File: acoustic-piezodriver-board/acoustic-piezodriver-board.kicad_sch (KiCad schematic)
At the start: 1 part, among them P301 WJ128V-5.0-3P

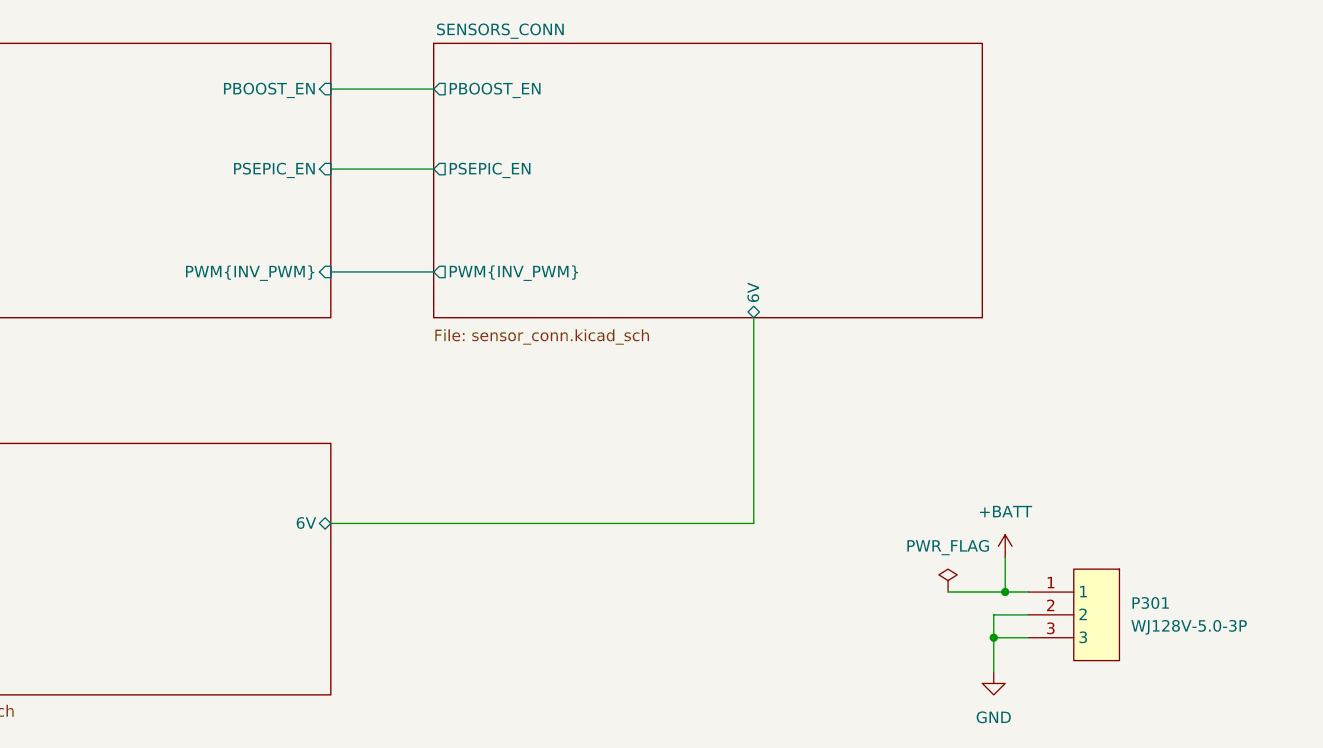
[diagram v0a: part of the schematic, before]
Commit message: [schematic] added adc for temperature measurement, current sense resistors, [layout] component placement, connector placement
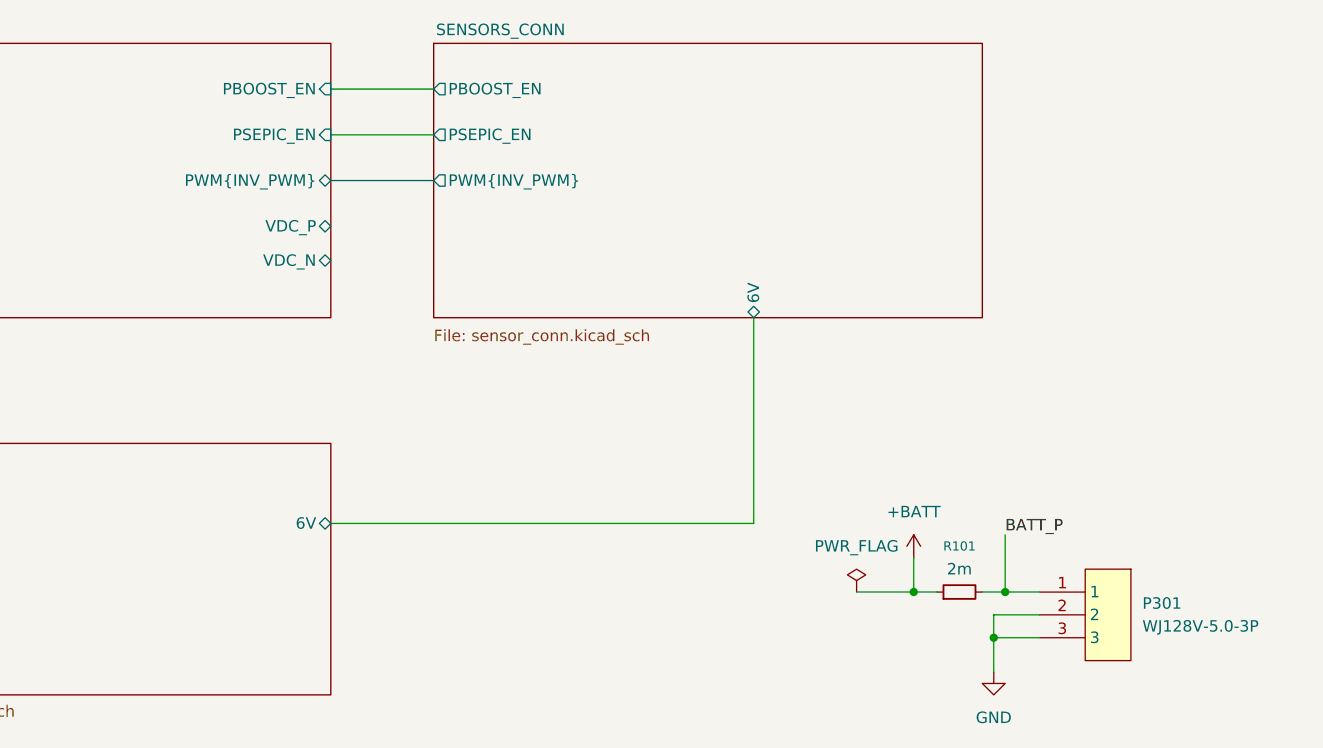
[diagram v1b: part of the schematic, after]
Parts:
- added R101: 2m, Resistor_SMD:R_2512_6332Metric, symbol Device:R_Small
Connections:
- net +BATT: now also R101.1; no longer P301.1
- new net BATT_P: P301.1, R101.2
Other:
- sheet INVERTER ports: added VDC_N, VDC_P; removed none
- moved on the sheet: P301

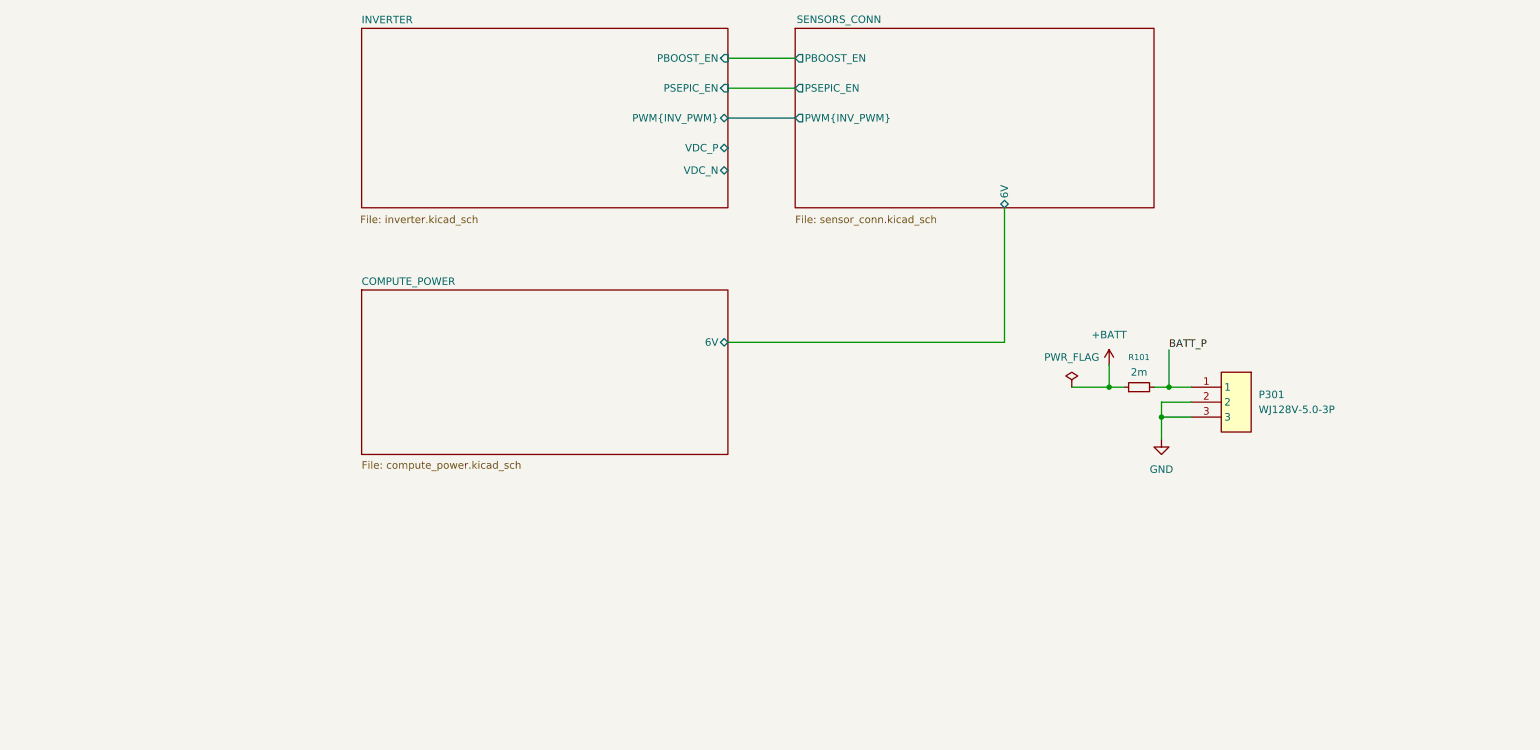
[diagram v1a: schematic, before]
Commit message: found hal-sensor, replaced with different one for lower voltage signal source impedance, reorganised schematic
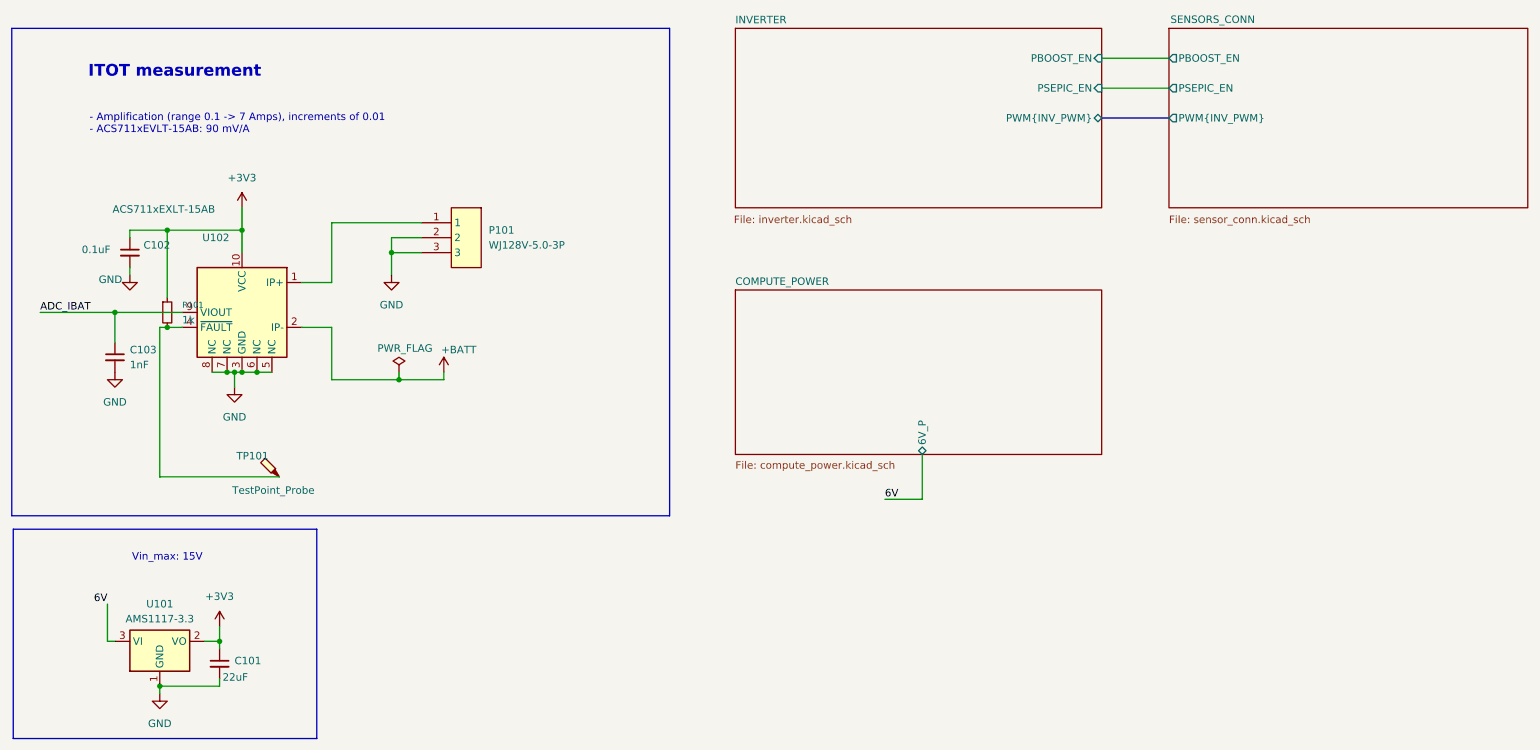
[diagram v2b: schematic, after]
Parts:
- removed P301: WJ128V-5.0-3P, iw-connector:WJ128V-5.0-3P, symbol iw-connector:WJ128V-5.0-3P
- added C101: 22uF, Capacitor_SMD:C_0805_2012Metric, symbol Device:C_Small
- added C102: 0.1uF, Capacitor_SMD:C_0402_1005Metric, symbol Device:C_Small
- added C103: 1nF, Capacitor_SMD:C_0402_1005Metric, symbol Device:C_Small
- added P101: WJ128V-5.0-3P, iw-connector:WJ128V-5.0-3P, symbol iw-connector:WJ128V-5.0-3P
- added TP101: TestPoint_Probe, TestPoint:TestPoint_Pad_D1.0mm, symbol Connector:TestPoint_Probe
- added U101: AMS1117-3.3, Package_TO_SOT_SMD:SOT-223-3_TabPin2, symbol Regulator_Linear:AMS1117-3.3
- added U102: ACS711xEXLT-15AB, Sensor_Current:Allegro_QFN-12-10-1EP_3x3mm_P0.5mm, symbol Sensor_Current:ACS711xEXLT-15AB
- R101: value 2m -> 1k; footprint Resistor_SMD:R_2512_6332Metric -> Resistor_SMD:R_0603_1608Metric; LPN C160590 -> C21190; MPN RLP25FEER002 -> 0603WAF1001T5E
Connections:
- net +BATT: now also U102.2 (IP-); no longer R101.1
- net GND: now also C101.2, C102.2, C103.2, P101.2, P101.3, U101.1 (GND), U102.3 (GND), U102.5 (NC), U102.6 (NC), U102.7 (NC), U102.8 (NC)
- net BATT_P: no longer names the net of R101.2
- net BATT_P: now also TP101.1, U102.4 (~{FAULT})
- new net: P101.1, U102.1 (IP+)
- new net +3V3: C101.1, C102.1, R101.1, U101.2 (VO), U102.10 (VCC)
- new net 6V: U101.3 (VI)
- new net ADC_IBAT: C103.1, U102.9 (VIOUT)
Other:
- sheet COMPUTE_POWER ports: added 6V_P; removed 6V
- sheet INVERTER ports: added none; removed VDC_N, VDC_P
- sheet SENSORS_CONN ports: added none; removed 6V
- note added: "- Amplification (range 0.1 -> 7 Amps), increments of 0.01 - ACS711xEVLT-15AB: 90 mV/A"
- note added: "ITOT measurement"
- note added: "Vin_max: 15V"

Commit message: added new notes + schematic component hal sensors
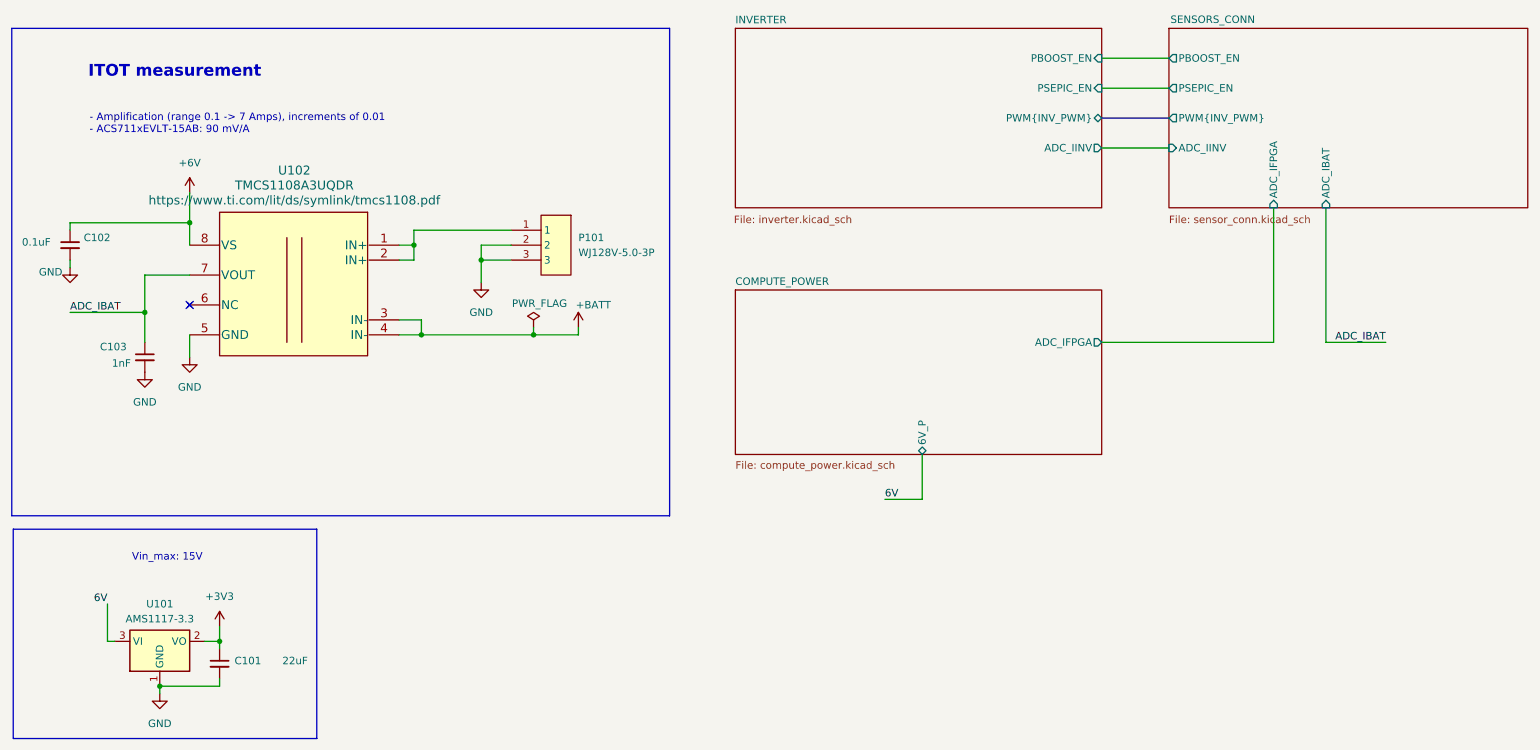
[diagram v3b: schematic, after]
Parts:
- removed R101: 1k, Resistor_SMD:R_0603_1608Metric, symbol Device:R_Small
- removed TP101: TestPoint_Probe, TestPoint:TestPoint_Pad_D1.0mm, symbol Connector:TestPoint_Probe
- removed U102: ACS711xEXLT-15AB, Sensor_Current:Allegro_QFN-12-10-1EP_3x3mm_P0.5mm, symbol Sensor_Current:ACS711xEXLT-15AB
- added U102: TMCS1108A3UQDR, iw-power:TMCS1108A3UQDR, symbol iw-power:TMCS1108A3UQDR
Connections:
- net +3V3: no longer C102.1
- net +BATT: now also U102.3 (IN-), U102.4 (IN-)
- net ADC_IBAT: now also U102.7 (VOUT)
- net GND: now also U102.5 (GND)
- net at P101.1: now also U102.1 (IN+), U102.2 (IN+)
- new net +6V: C102.1, U102.8 (VS)
- no-connect marks 0 -> 1
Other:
- sheet COMPUTE_POWER ports: added ADC_IFPGA; removed none
- sheet INVERTER ports: added ADC_IINV; removed none
- sheet SENSORS_CONN ports: added ADC_IBAT, ADC_IFPGA, ADC_IINV; removed none
- moved on the sheet: C102, C103, P101

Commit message: finished schematic, routing
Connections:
- net 6V is gone; now on net +6V: U101.3 (VI)
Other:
- sheet COMPUTE_POWER ports: added none; removed 6V_P
- note added: "Vin_max: 15V, I_max: 1 A - 2 temperature sensors - 1 ADC"
- note removed: "Vin_max: 15V"
- moved on the sheet: C101, U101
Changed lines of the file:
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@@
 	(paper "A4")
 	(rectangle
-		(start 18.288 130.81)
-		(end 69.85 166.37)
+		(start 18.288 128.27)
+		(end 69.85 163.83)
 		(stroke
 			(width 0)
@@
 	(rectangle
 		(start 18.034 45.72)
-		(end 129.794 128.524)
+		(end 129.794 118.11)
 		(stroke
 			(width 0)
@@
 		)
 	)
-	(text "Vin_max: 15V"
-		(exclude_from_sim no)
-		(at 44.45 135.636 0)
+	(text "Vin_max: 15V, I_max: 1 A\n- 2 temperature sensors\n- 1 ADC"
+		(exclude_from_sim no)
+		(at 19.05 133.858 0)
 		(effects
 			(font
 				(size 1.27 1.27)
 			)
+			(justify left)
 		)
 	)
@@
 	)
 	(junction
-		(at 53.34 149.86)
+		(at 53.34 147.32)
 		(diameter 0)
 		(color 0 0 0 0)
 	)
 	(junction
-		(at 43.18 157.48)
+		(at 43.18 154.94)
 		(diameter 0)
 		(color 0 0 0 0)
@@
 	(wire
 		(pts
+			(xy 34.29 144.78) (xy 34.29 147.32)
+		)
+		(stroke
+			(width 0)
+			(type default)
+		)
+	)
+	(wire
+		(pts
 			(xy 106.68 96.52) (xy 106.68 97.79)
 		)
@@
 	(wire
 		(pts
-			(xy 53.34 147.32) (xy 53.34 149.86)
+			(xy 53.34 144.78) (xy 53.34 147.32)
 		)
 		(stroke
@@
 	(wire
 		(pts
-			(xy 50.8 149.86) (xy 53.34 149.86)
+			(xy 50.8 147.32) (xy 53.34 147.32)
 		)
 		(stroke
@@
 	(wire
 		(pts
-			(xy 53.34 157.48) (xy 43.18 157.48)
+			(xy 53.34 154.94) (xy 43.18 154.94)
 		)
 		(stroke
@@
 	(wire
 		(pts
-			(xy 34.29 143.51) (xy 34.29 149.86)
-		)
-		(stroke
-			(width 0)
-			(type default)
-		)
-	)
-	(wire
-		(pts
-			(xy 34.29 149.86) (xy 35.56 149.86)
-		)
-		(stroke
-			(width 0)
-			(type default)
-		)
-	)
-	(wire
-		(pts
 			(xy 27.94 78.74) (xy 48.26 78.74)
 		)
@@
 	(wire
 		(pts
-			(xy 43.18 157.48) (xy 43.18 158.75)
+			(xy 43.18 154.94) (xy 43.18 156.21)
 		)
 		(stroke
@@
 	(wire
 		(pts
-			(xy 53.34 151.13) (xy 53.34 149.86)
+			(xy 53.34 148.59) (xy 53.34 147.32)
 		)
 		(stroke
@@
 	(wire
 		(pts
-			(xy 53.34 156.21) (xy 53.34 157.48)
+			(xy 53.34 153.67) (xy 53.34 154.94)
 		)
 		(stroke
@@
 	(wire
 		(pts
+			(xy 34.29 147.32) (xy 35.56 147.32)
+		)
+		(stroke
+			(width 0)
+			(type default)
+		)
+	)
+	(wire
+		(pts
 			(xy 48.26 101.6) (xy 48.26 97.79)
 		)
@@
 	(wire
 		(pts
-			(xy 172.72 125.73) (xy 172.72 118.11)
-		)
-		(stroke
-			(width 0)
-			(type default)
-		)
-	)
-	(wire
-		(pts
 			(xy 86.36 80.01) (xy 86.36 82.55)
-		)
-		(stroke
-			(width 0)
-			(type default)
-		)
-	)
-	(wire
-		(pts
-			(xy 166.37 125.73) (xy 172.72 125.73)
 		)
 		(stroke
@@
 	(label "ADC_IBAT"
 		(at 251.46 99.06 180)
-		(effects
-			(font
-				(size 1.27 1.27)
-			)
-			(justify right bottom)
-		)
-	)
-	(label "6V"
-		(at 166.37 125.73 0)
-		(effects
-			(font
-				(size 1.27 1.27)
-			)
-			(justify left bottom)
-		)
-	)
-	(label "6V"
-		(at 34.29 143.51 180)
 		(effects
 			(font
@@
 	(symbol
 		(lib_id "power:GND")
-		(at 43.18 158.75 0)
+		(at 43.18 156.21 0)
 		(unit 1)
 		(exclude_from_sim no)
@@
 		(fields_autoplaced yes)
 		(property "Reference" "#PWR0104"
-			(at 43.18 165.1 0)
+			(at 43.18 162.56 0)
 			(effects
 				(font
@@
 		)
 		(property "Value" "GND"
-			(at 43.18 163.83 0)
+			(at 43.18 161.29 0)
 			(effects
 				(font
@@
 		)
 		(property "Footprint" ""
-			(at 43.18 158.75 0)
+			(at 43.18 156.21 0)
 			(effects
 				(font
@@
 		)
 		(property "Datasheet" ""
-			(at 43.18 158.75 0)
+			(at 43.18 156.21 0)
 			(effects
 				(font
@@
 		)
 		(property "Description" "Power symbol creates a global label with name \"GND\" , ground"
-			(at 43.18 158.75 0)
+			(at 43.18 156.21 0)
 			(effects
 				(font
@@
 	(symbol
 		(lib_id "power:+3V3")
-		(at 53.34 147.32 0)
+		(at 53.34 144.78 0)
 		(unit 1)
 		(exclude_from_sim no)
@@
 		(fields_autoplaced yes)
 		(property "Reference" "#PWR0103"
-			(at 53.34 151.13 0)
+			(at 53.34 148.59 0)
 			(effects
 				(font
@@
 		)
 		(property "Value" "+3V3"
-			(at 53.34 142.24 0)
+			(at 53.34 139.7 0)
 			(effects
 				(font
@@
 		)
 		(property "Footprint" ""
-			(at 53.34 147.32 0)
+			(at 53.34 144.78 0)
 			(effects
 				(font
@@
 		)
 		(property "Datasheet" ""
-			(at 53.34 147.32 0)
+			(at 53.34 144.78 0)
 			(effects
 				(font
@@
 		)
 		(property "Description" "Power symbol creates a global label with name \"+3V3\""
-			(at 53.34 147.32 0)
+			(at 53.34 144.78 0)
 			(effects
 				(font
@@
 	(symbol
 		(lib_id "Regulator_Linear:AMS1117-3.3")
-		(at 43.18 149.86 0)
+		(at 43.18 147.32 0)
 		(unit 1)
 		(exclude_from_sim no)
@@
 		(fields_autoplaced yes)
 		(property "Reference" "U101"
+			(at 43.18 140.97 0)
+			(effects
+				(font
+					(size 1.27 1.27)
+				)
+			)
+		)
+		(property "Value" "AMS1117-3.3"
 			(at 43.18 143.51 0)
 			(effects
@@
 			)
 		)
-		(property "Value" "AMS1117-3.3"
-			(at 43.18 146.05 0)
-			(effects
-				(font
-					(size 1.27 1.27)
-				)
-			)
-		)
 		(property "Footprint" "Package_TO_SOT_SMD:SOT-223-3_TabPin2"
-			(at 43.18 144.78 0)
+			(at 43.18 142.24 0)
 			(effects
 				(font
@@
 		)
 		(property "Datasheet" "http://www.advanced-monolithic.com/pdf/ds1117.pdf"
-			(at 45.72 156.21 0)
+			(at 45.72 153.67 0)
 			(effects
 				(font
@@
 		)
 		(property "Description" "1A Low Dropout regulator, positive, 3.3V fixed output, SOT-223"
-			(at 43.18 149.86 0)
+			(at 43.18 147.32 0)
 			(effects
 				(font
@@
 		)
 		(property "LPN" "C6186"
-			(at 43.18 149.86 0)
+			(at 43.18 147.32 0)
 			(effects
 				(font
@@
 		)
 		(property "MPN" "AMS1117-3.3 "
-			(at 43.18 149.86 0)
+			(at 43.18 147.32 0)
 			(effects
 				(font
@@
 	)
 	(symbol
+		(lib_id "power:+6V")
+		(at 34.29 144.78 0)
+		(unit 1)
+		(exclude_from_sim no)
+		(in_bom yes)
+		(on_board yes)
+		(dnp no)
+		(fields_autoplaced yes)
+		(property "Reference" "#PWR0107"
+			(at 34.29 148.59 0)
+			(effects
+				(font
+					(size 1.27 1.27)
+				)
+				(hide yes)
+			)
+		)
+		(property "Value" "+6V"
+			(at 34.29 139.7 0)
+			(effects
+				(font
+					(size 1.27 1.27)
+				)
+			)
+		)
+		(property "Footprint" ""
+			(at 34.29 144.78 0)
+			(effects
+				(font
+					(size 1.27 1.27)
+				)
+				(hide yes)
+			)
+		)
+		(property "Datasheet" ""
+			(at 34.29 144.78 0)
+			(effects
+				(font
+					(size 1.27 1.27)
+				)
+				(hide yes)
+			)
+		)
+		(property "Description" "Power symbol creates a global label with name \"+6V\""
+			(at 34.29 144.78 0)
+			(effects
+				(font
+					(size 1.27 1.27)
+				)
+				(hide yes)
+			)
+		)
+		(pin "1"
+		)
+		(instances
+			(project ""
+				(path "/94cb090f-214e-44cc-b8ed-ae50ff29d2bf"
+					(reference "#PWR0107")
+					(unit 1)
+				)
+			)
+		)
+	)
+	(symbol
 		(lib_id "Device:C_Small")
-		(at 53.34 153.67 0)
+		(at 53.34 151.13 0)
 		(unit 1)
 		(exclude_from_sim no)
@@
 		(dnp no)
 		(property "Reference" "C101"
-			(at 55.88 153.162 0)
+			(at 55.88 150.622 0)
 			(effects
 				(font
@@
 		)
 		(property "Value" "22uF"
-			(at 64.008 153.162 0)
+			(at 64.008 150.622 0)
 			(effects
 				(font
@@
 		)
 		(property "Footprint" "Capacitor_SMD:C_0805_2012Metric"
-			(at 53.34 153.67 0)
+			(at 53.34 151.13 0)
 			(effects
 				(font
@@
 		)
 		(property "Datasheet" "https://jlcpcb.com/api/file/downloadByFileSystemAccessId/8579706866429190144"
-			(at 53.34 153.67 0)
+			(at 53.34 151.13 0)
 			(effects
 				(font
@@
 		)
 		(property "Description" "X5R, 25V"
-			(at 53.34 153.67 0)
+			(at 53.34 151.13 0)
 			(effects
 				(font
@@
 		)
 		(property "LPN" "C45783"
-			(at 53.34 153.67 0)
+			(at 53.34 151.13 0)
 			(effects
 				(font
@@
 		)
 		(property "MPN" "CL21A226MAQNNNE"
-			(at 53.34 153.67 0)
+			(at 53.34 151.13 0)
 			(effects
 				(font
@@
 			)
 		)
-		(pin "6V_P" bidirectional
-			(at 172.72 118.11 270)
-			(effects
-				(font
-					(size 1.27 1.27)
-				)
-				(justify left)
-			)
-		)
